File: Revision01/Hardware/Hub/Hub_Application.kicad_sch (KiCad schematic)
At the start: 81 parts, among them J10 IDC 6Pin Male Header, J11 IDC 6Pin Male Header, J12 IDC 6Pin Male Header, J13 IDC 6Pin Male Header, J14 IDC 6Pin Male Header, J15 IDC 6Pin Female Socket, J16 IDC 6Pin Male Header, J17 IDC 6Pin Female Socket, J18 IDC 6Pin Female Socket, J19 SMA-J-P-H-ST-EM1, J6 IDC 6Pin Male Header, J7 IDC 6Pin Male Header, J8 IDC 6Pin Male Header, J9 IDC 6Pin Male Header, Q1 PMOS, Q2 NMOS, Q3 PMOS, U3 MPU-6500, U4 Adafruit 3070

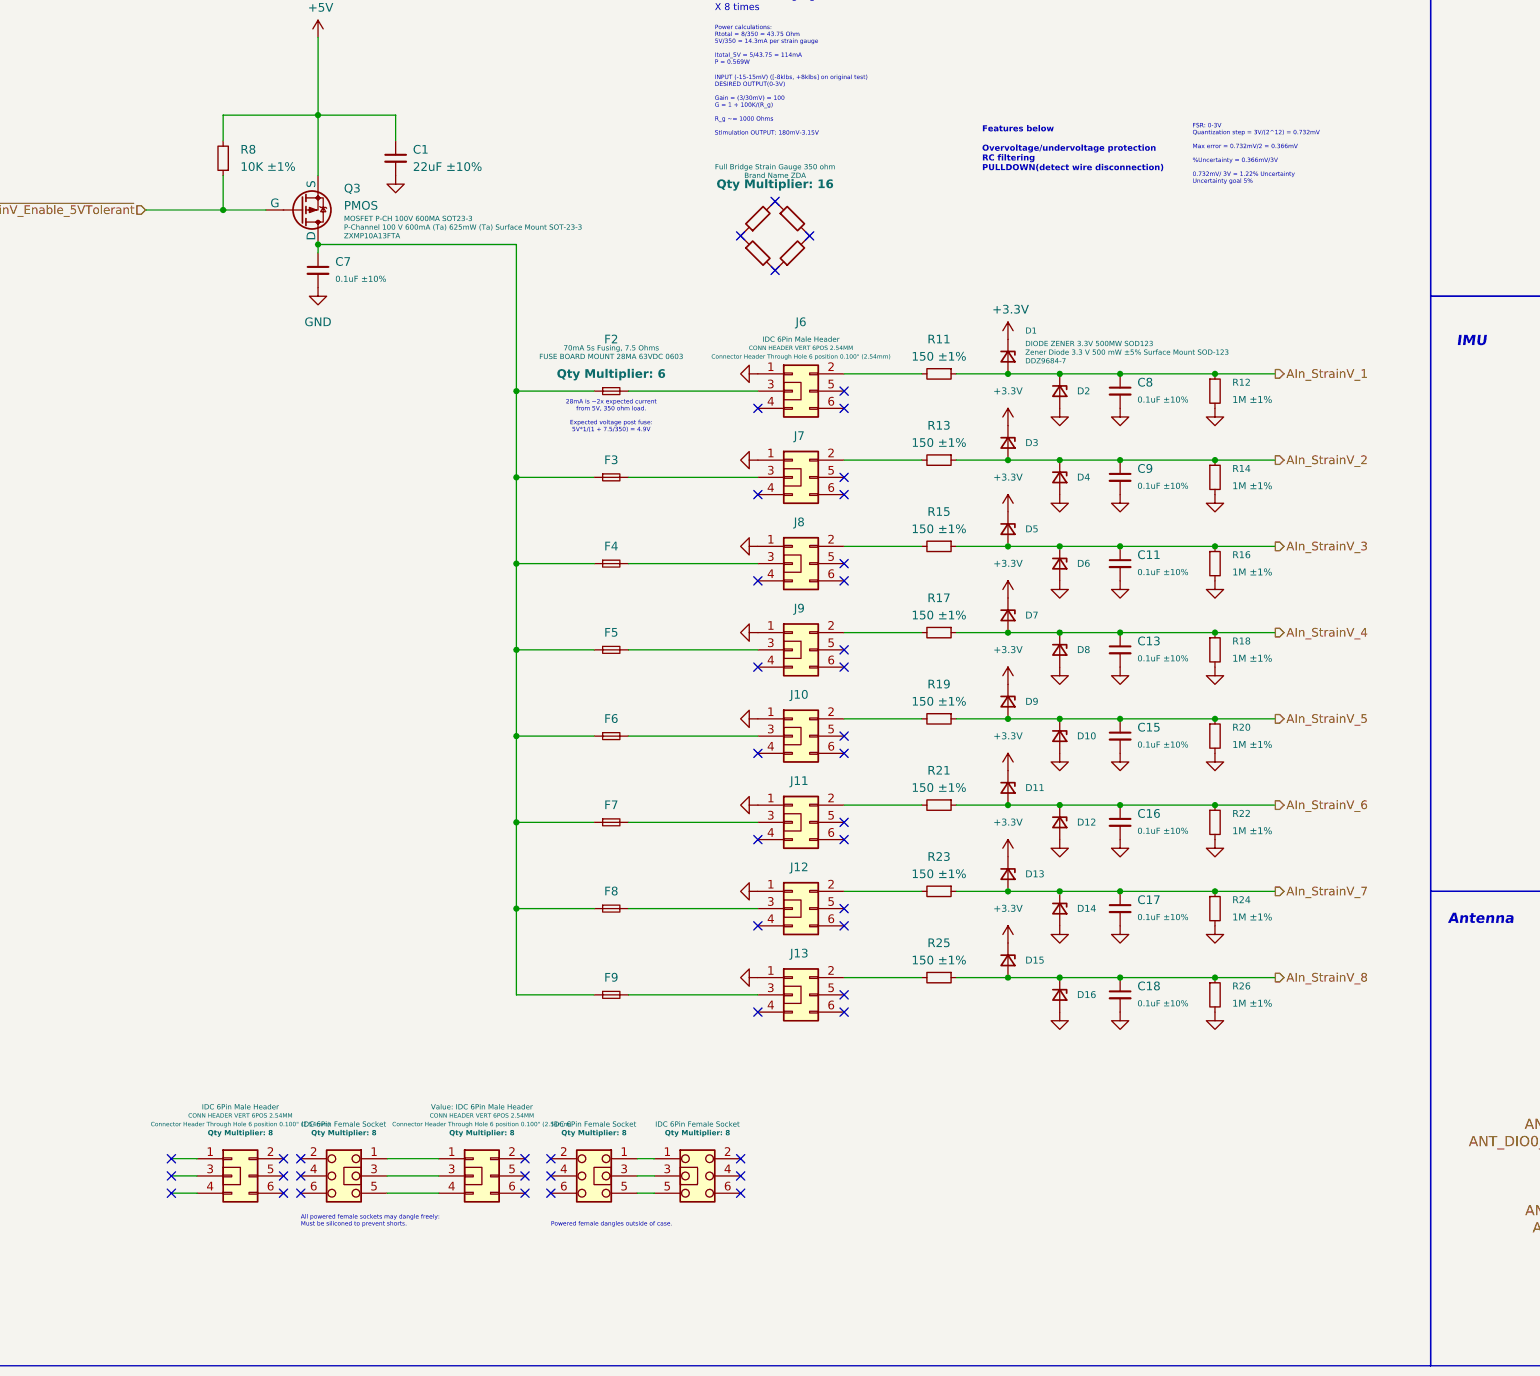
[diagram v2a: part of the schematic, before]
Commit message: . Moved R from main board to amplifier board to current limit the INA amplifier in case of cable short to GND . replaced RC filter with 500ohm, 6.8nF, in order to current limit the INA amplifier to 10mA, keeping a ~40-50kHz 3db frequency. . Reworked Hub layout. . Reworked Hub component columns for Digikey, Mouser, & Aliexpress.
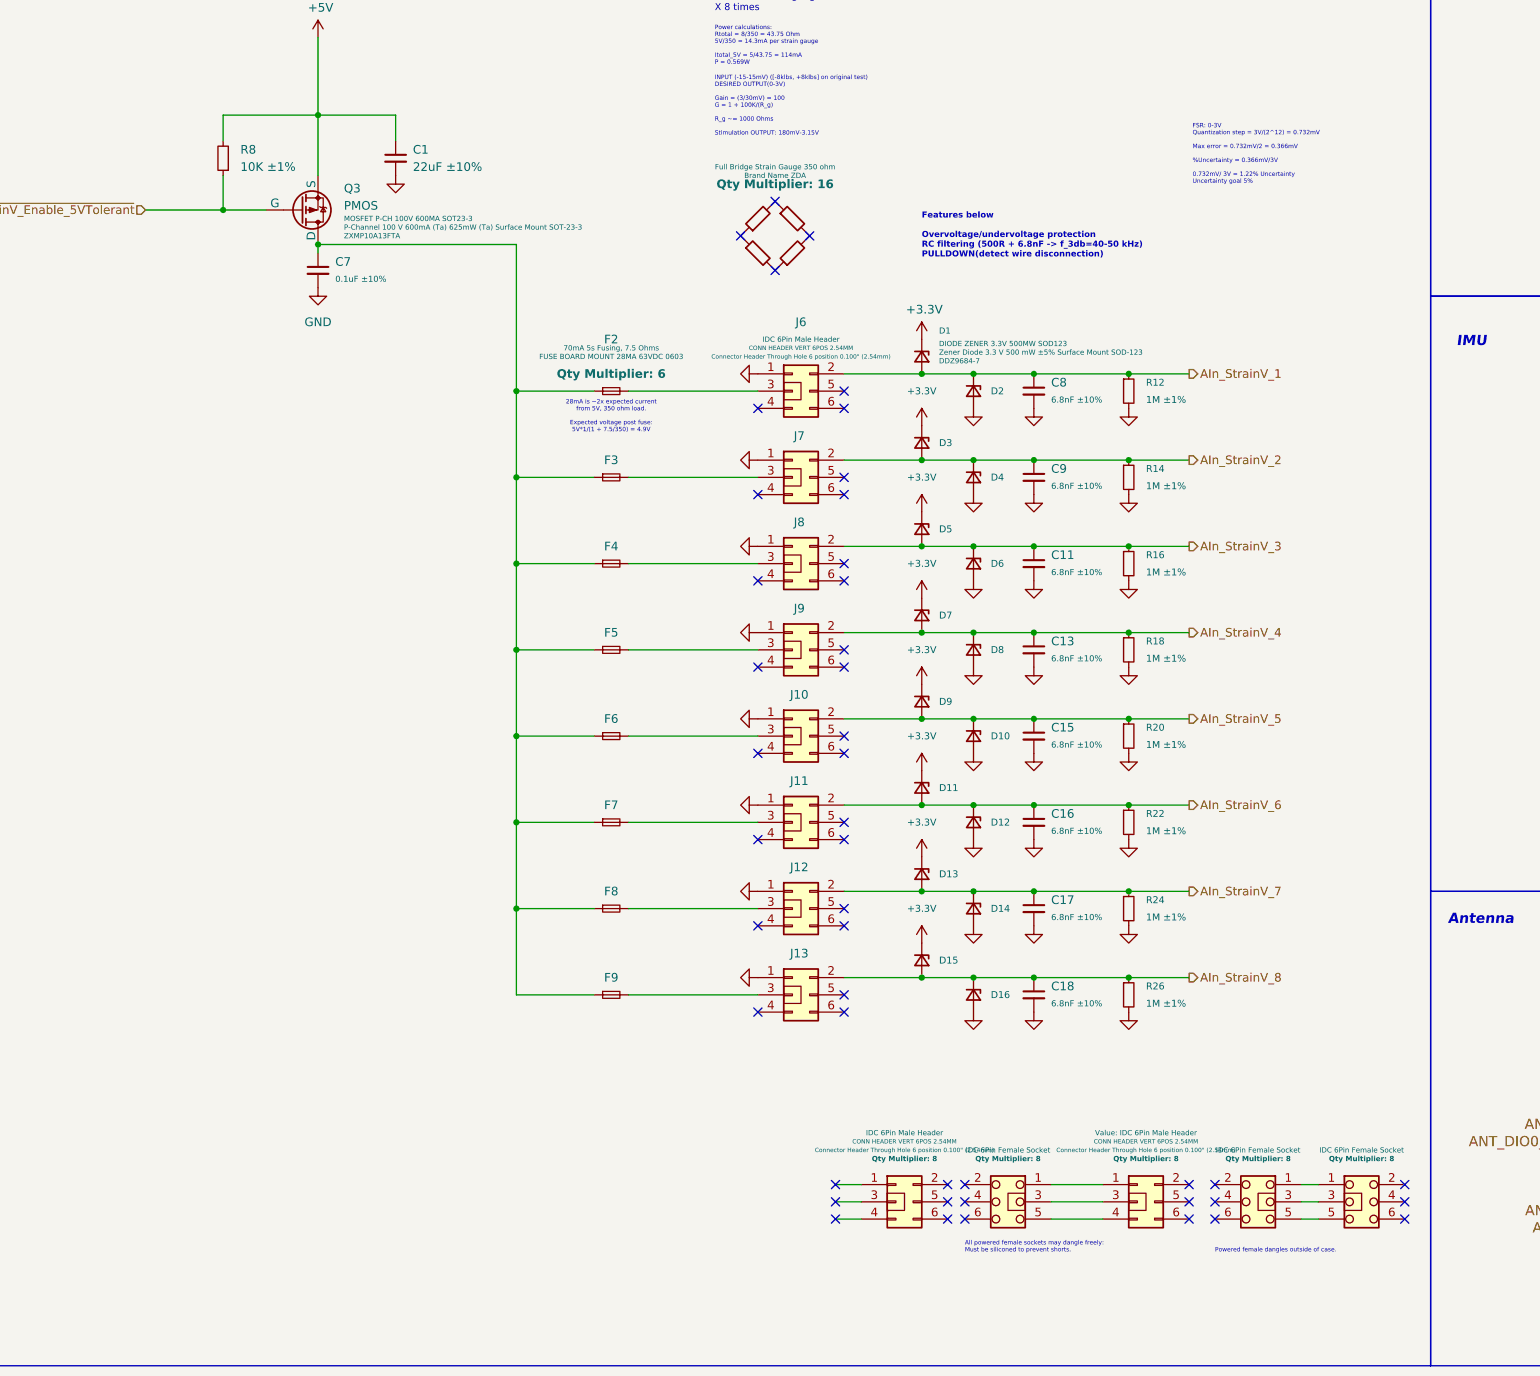
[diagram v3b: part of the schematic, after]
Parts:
- removed R11, R13, R15, R17, R19, R21, R23, R25: 150 ±1%, Resistor_SMD:R_0805_2012Metric_Pad1.20x1.40mm_HandSolder, symbol Device:R_Small
- C11, C13, C15, C16, C17, C18, C8, C9: value 0.1uF ±10% -> 6.8nF ±10%; footprint Capacitor_SMD:C_0805_2012Metric_Pad1.18x1.45mm_HandSolder -> Capacitor_SMD:C_0603_1608Metric_Pad1.08x0.95mm_HandSolder; Detailed Description 0.1 µF ±10% 100V Ceramic Capacitor X7R 0805 (2012 Metric) -> Multilayer Ceramic Capacitors MLCC - SMD/SMT 6.8nF+/-10% 50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; DigiKey Link https://www.digikey.ca/en/products/detail/samsung-electro-m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 -> (none); DigiKey Part Number 1276-6840-1-ND - Cut Tape (CT) -> (none); Manufacturer Part Number CL21B104KCFNNNE -> CL10B682KB8NNNC; Mouser Link (none) -> https://mou.sr/3J8ffq3; Mouser Part Number (none) -> 187-CL10B682KB8NNNC; Package 0805 (2012 Metric) -> 0603 (1608 metric)
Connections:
- net AIn_StrainV_1: now also J6.2 (Pin_2)
- net AIn_StrainV_2: now also J7.2 (Pin_2)
- net AIn_StrainV_3: now also J8.2 (Pin_2)
- net AIn_StrainV_4: now also J9.2 (Pin_2)
- net AIn_StrainV_5: now also J10.2 (Pin_2)
- net AIn_StrainV_6: now also J11.2 (Pin_2)
- net AIn_StrainV_7: now also J12.2 (Pin_2)
- net AIn_StrainV_8: now also J13.2 (Pin_2)
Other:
- note added: "Features below Overvoltage/undervoltage protection RC filtering (500R + 6.8nF -> f_3db=40-50 kHz) PULLDOWN(detect wire disconnection)"
- note removed: "Features below Overvoltage/undervoltage protection RC filtering PULLDOWN(detect wire disconnection)"
- moved on the sheet: C8, D1, D10, D11, D12, D13, D14, D15, D16, D2, D3, D4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

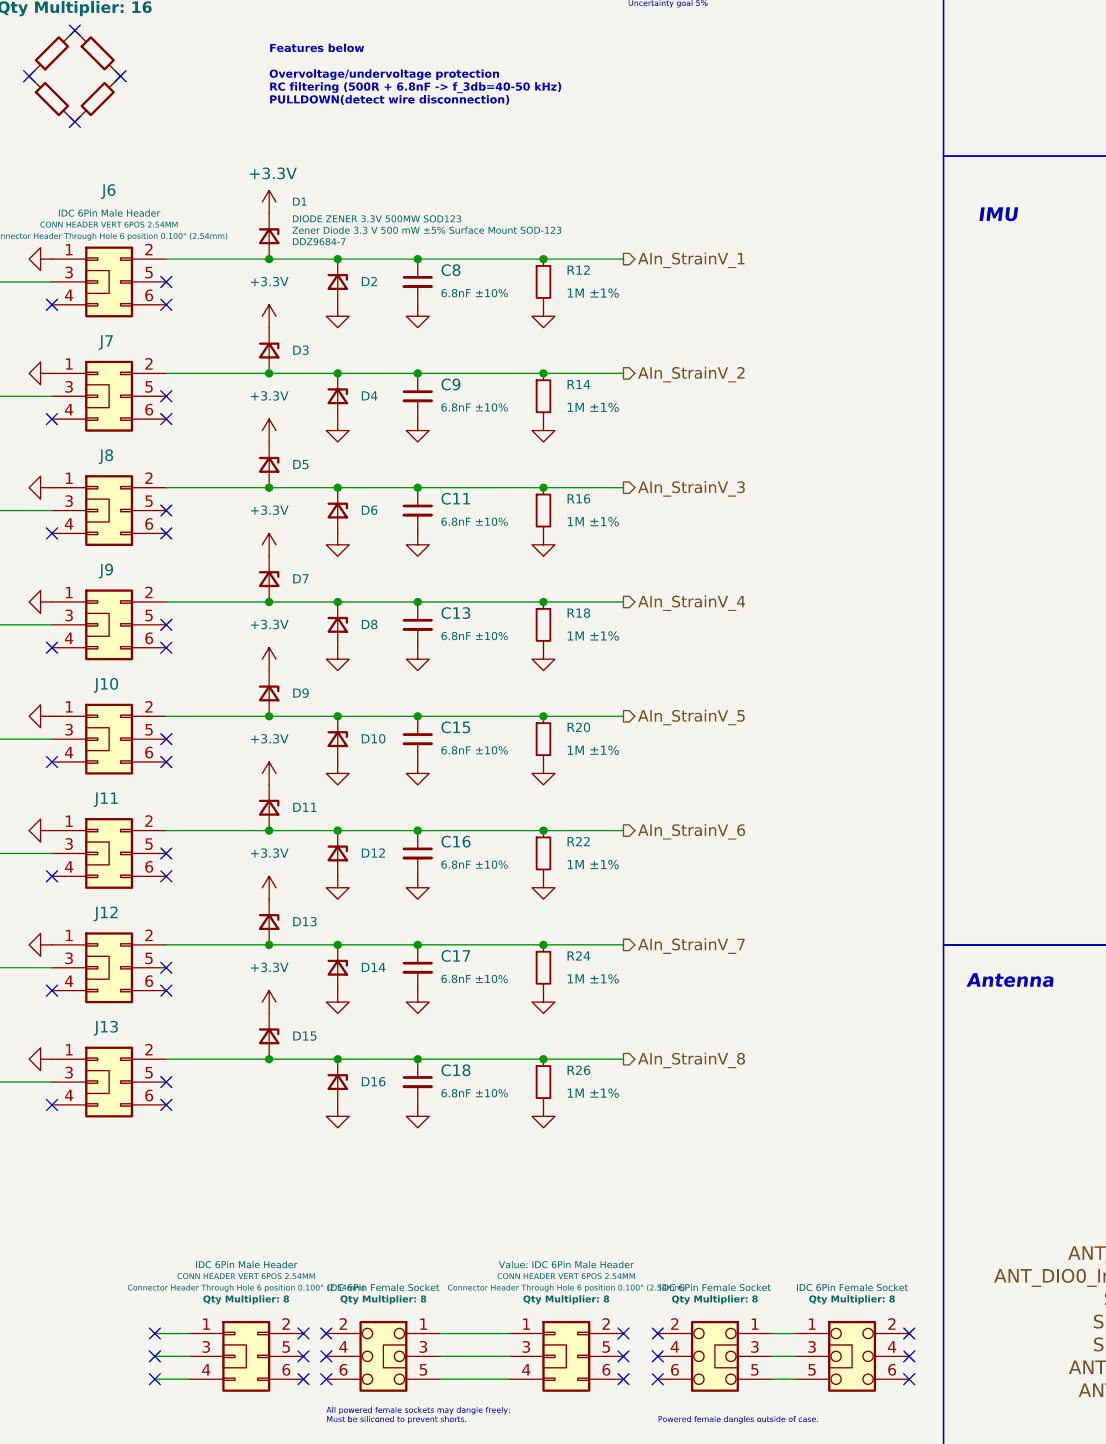
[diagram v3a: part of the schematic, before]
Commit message: . Amplifier layout WIP draft with 500 ohm resistor . Hub layout final draft, added 100 ohm series resistor to AIN
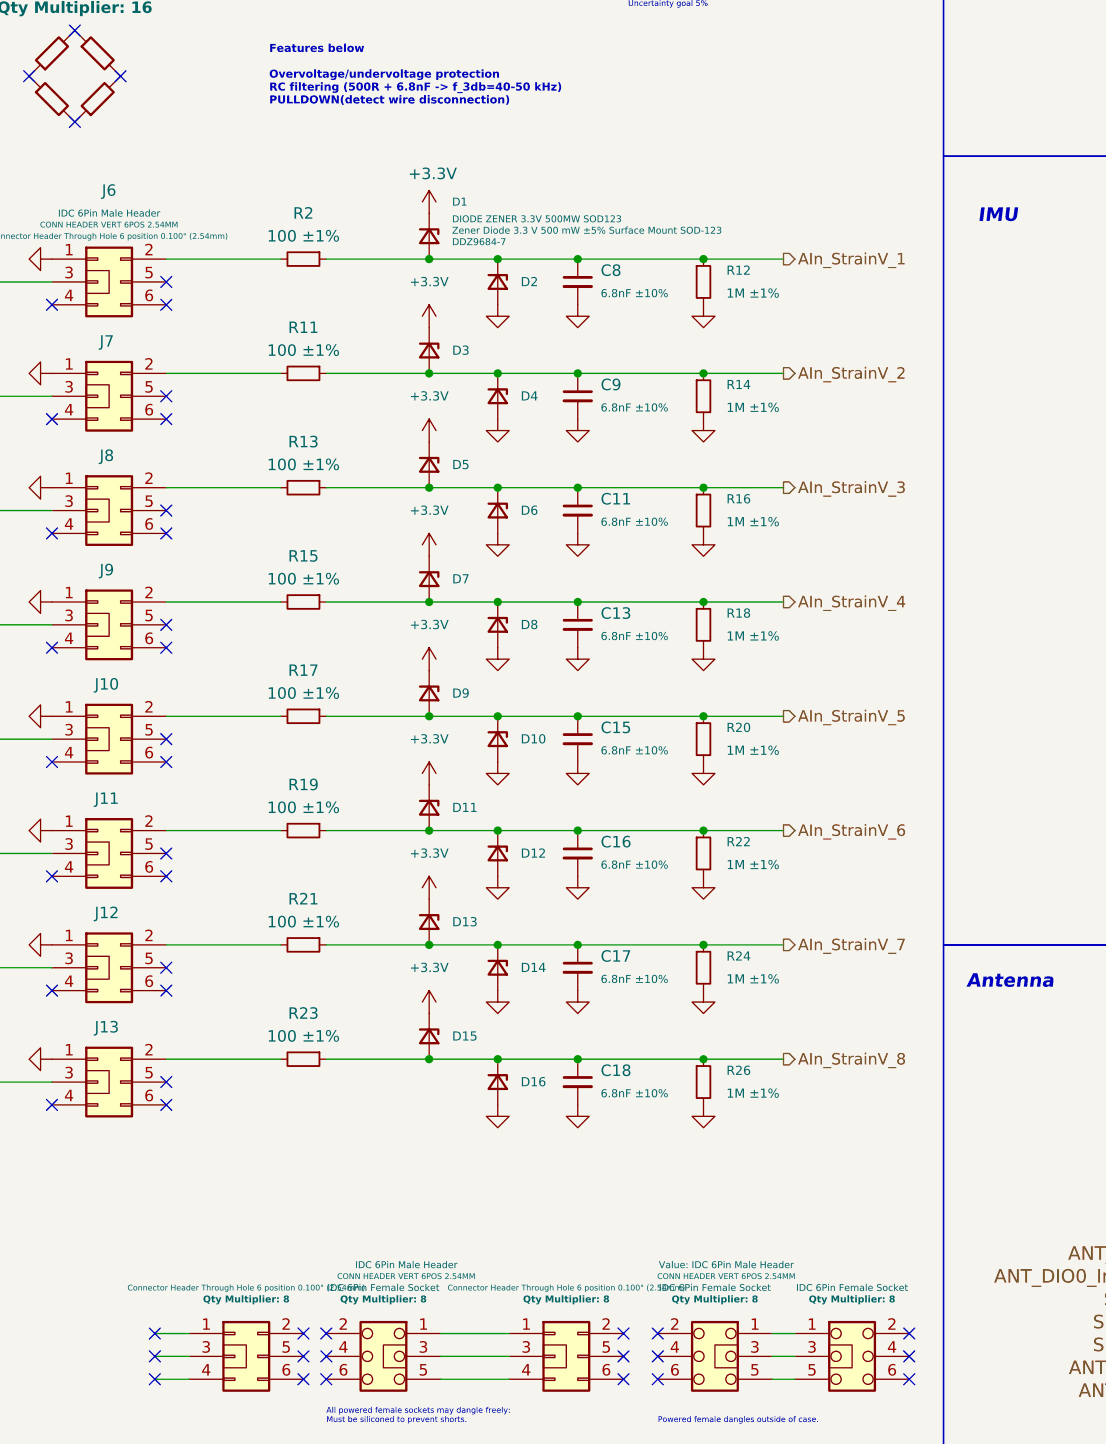
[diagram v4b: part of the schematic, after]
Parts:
- added R11, R13, R15, R17, R19, R2, R21, R23: 100 ±1%, Resistor_SMD:R_0805_2012Metric_Pad1.20x1.40mm_HandSolder, symbol Device:R_Small
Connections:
- net AIn_StrainV_1: now also R2.1; no longer J6.2 (Pin_2)
- net AIn_StrainV_2: now also R11.1; no longer J7.2 (Pin_2)
- net AIn_StrainV_3: now also R13.1; no longer J8.2 (Pin_2)
- net AIn_StrainV_4: now also R15.1; no longer J9.2 (Pin_2)
- net AIn_StrainV_5: now also R17.1; no longer J10.2 (Pin_2)
- net AIn_StrainV_6: now also R19.1; no longer J11.2 (Pin_2)
- net AIn_StrainV_7: now also R21.1; no longer J12.2 (Pin_2)
- net AIn_StrainV_8: now also R23.1; no longer J13.2 (Pin_2)
- new net: J7.2 (Pin_2), R11.2
- new net: J9.2 (Pin_2), R15.2
- new net: J6.2 (Pin_2), R2.2
- new net: J8.2 (Pin_2), R13.2
- new net: J13.2 (Pin_2), R23.2
- new net: J10.2 (Pin_2), R17.2
- new net: J12.2 (Pin_2), R21.2
- new net: J11.2 (Pin_2), R19.2
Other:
- moved on the sheet: C11, C13, C15, C16, C17, C18, C8, C9, D1, D10, D11, D12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
